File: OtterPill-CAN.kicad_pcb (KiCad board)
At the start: 2 copper layers, 30.8 x 17.6 mm, 19 parts, among them J1 pinh, J2 pinh, J3 CAN, J5 SWD, J7 PAD, U1 TJA1051T-3

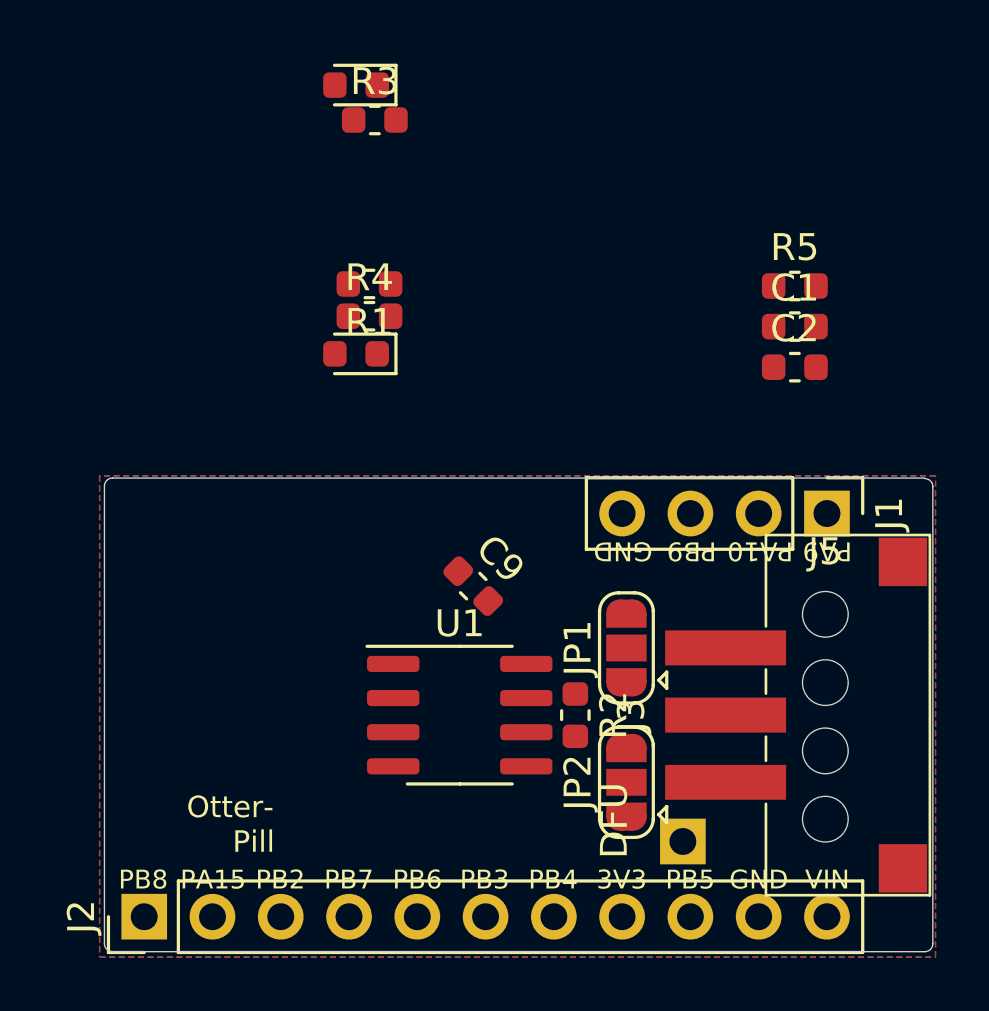
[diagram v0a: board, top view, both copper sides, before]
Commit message: finalized schematic
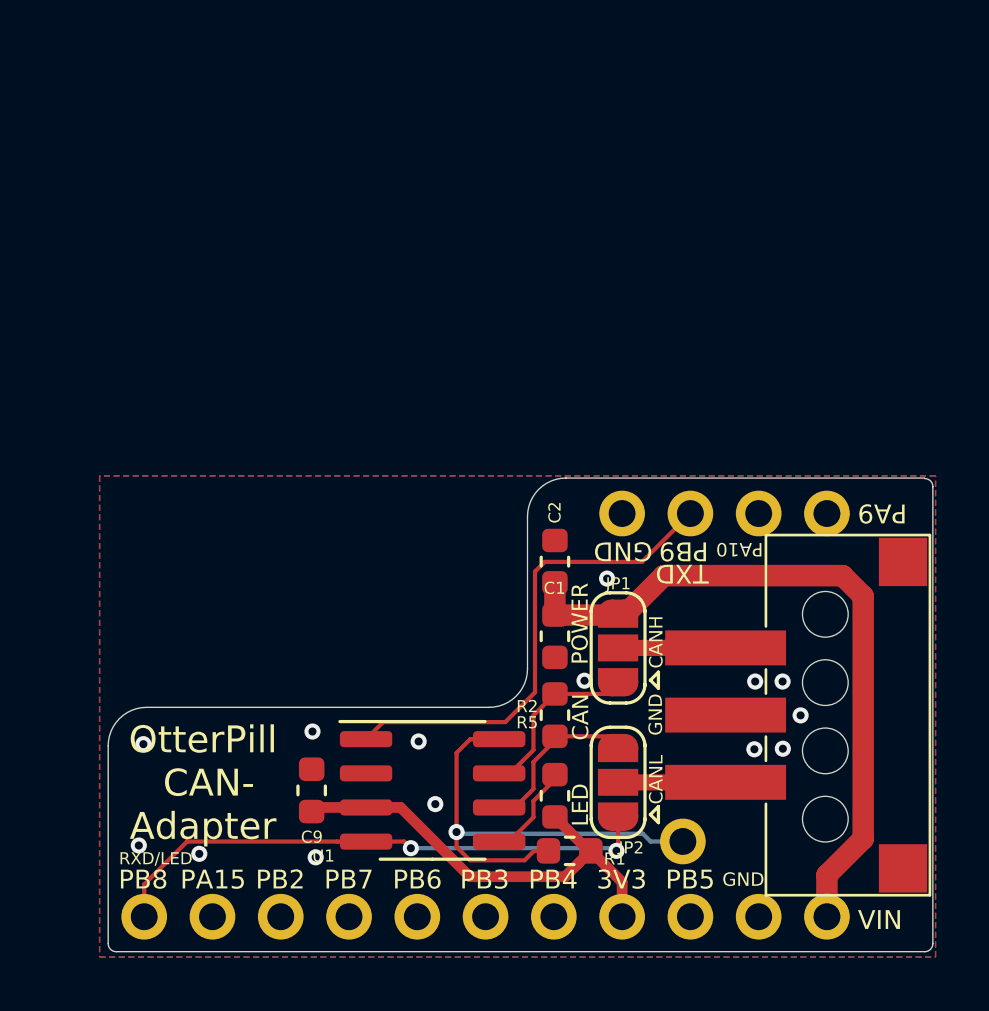
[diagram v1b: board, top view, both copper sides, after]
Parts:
- removed D1: LED RED, LED_SMD:LED_0603_1608Metric
- removed D2: LED GREEN, LED_SMD:LED_0603_1608Metric
- removed R3, R4: 3k3, Resistor_SMD:R_0603_1608Metric
- J1: footprint Connector_PinHeader_2.54mm:PinHeader_1x04_P2.54mm_Vertical -> otter:PinHeader_1x04_P2.54mm_Vertical_NOSILK
- J2: footprint Connector_PinHeader_2.54mm:PinHeader_1x11_P2.54mm_Vertical -> otter:PinHeader_1x11_P2.54mm_Vertical_NOSILK
- J7: footprint Connector_PinHeader_2.54mm:PinHeader_1x01_P2.54mm_Vertical -> otter:PinHeader_1x01_P2.54mm_Vertical_NOSILK
- moved G*** 31.8 mm to (55.1, 55.3)
- moved R1 22.4 mm to (49.7, 33.6)
- moved R5 21.0 mm to (49.1, 31.6), turned to 270 degrees
- moved C1 14.6 mm to (49.1, 25.7), turned to 270 degrees
- moved C2 11.5 mm to (49.1, 22.9), turned to 90 degrees
- moved C9 9.69 mm to (40.1, 31.4), turned to 90 degrees
- moved U1 2.98 mm to (44.6, 31.4)
- moved R2 0.76 mm to (49.1, 28.6)
- moved JP1 0.31 mm to (51.5, 26.1)
- moved JP2 0.31 mm to (51.5, 31.1)
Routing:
- net VIN: track 0.00 -> 26.1 mm
- net RXD: track 0.00 -> 21.0 mm, vias 0 -> 2
- net TXD: track 0.00 -> 18.2 mm
- net Net-(J7-Pad1): track 0.00 -> 17.6 mm, vias 0 -> 1
- net +3V3: track 0.00 -> 16.7 mm
- net Net-(JP1-Pad1): track 0.00 -> 6.88 mm
- net Net-(JP2-Pad3): track 0.00 -> 6.68 mm
- net CAN_L: track 0.00 -> 3.69 mm
- net CAN_H: track 0.00 -> 3.69 mm
- net Net-(R5-Pad1): track 0.00 -> 3.57 mm
- net GND: vias 0 -> 14
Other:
- board size 30.8 x 17.6 mm -> 30.7 x 17.6 mm
- board text added: "CAN"
- board text added: "CANH"
- board text added: "CANL"
- board text added: "LED"
- board text added: "OtterPill CAN- Adapter"
- board text added: "POWER"
- board text added: "RXD/LED"
- board text added: "TXD"
- board text removed: "DFU"
- board text removed: "Otter- Pill"

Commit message: finalized layout
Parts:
- removed C1, C2: 100n 50V, Capacitor_SMD:C_0603_1608Metric
- removed G***: LOGO, otter:otter_laying_3411
- removed JP1: VIN, Jumper:SolderJumper-3_P1.3mm_Open_RoundedPad1.0x1.5mm
- removed JP2: WS2812, Jumper:SolderJumper-3_P1.3mm_Open_RoundedPad1.0x1.5mm
- moved J1 15.0 mm to (59.3, 36.1)
- moved J2 15.0 mm to (33.9, 21.1)
- moved J7 9.40 mm to (53.9, 23.9)
- moved R1 8.86 mm to (51.4, 24.9), turned to 270 degrees
- moved C9 5.87 mm to (42.3, 26.0)
- moved U1 5.87 mm to (46.7, 25.9)
- moved R5 2.33 mm to (51.4, 30.9)
- moved R2 2.32 mm to (51.4, 27.9)
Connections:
- R2 pad 1: Net-(JP1-Pad1) -> CAN_H
- R2 pad 2: Net-(JP2-Pad3) -> CAN_L
- U1 pad 6: Net-(JP2-Pad3) -> CAN_L
- U1 pad 7: Net-(JP1-Pad1) -> CAN_H
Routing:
- net VIN: track 26.1 -> 0.00 mm
- net +3V3: track 16.7 -> 32.5 mm, vias 0 -> 2
- net Net-(J7-Pad1): track 17.6 -> 6.62 mm, vias 1 -> 0
- net Net-(JP1-Pad1): track 6.88 -> 0.00 mm
- net Net-(JP2-Pad3): track 6.68 -> 0.00 mm
- net RXD: track 21.0 -> 15.4 mm, vias 2 -> 0
- net CAN_L: track 3.69 -> 8.57 mm
- net CAN_H: track 3.69 -> 7.64 mm
- net GND: vias 14 -> 17
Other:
- outline, holes or cut-outs redrawn
- rule pad_to_mask_clearance: 0.01 -> 0
- board text added: "Jan Henrik 2019"
- board text removed: "CAN"
- board text removed: "Jan Henrik 2019 v1.2"
- board text removed: "LED"
- board text removed: "Otterpill"
- board text removed: "POWER"
- board text removed: "RXD/LED"
- board text removed: "TXD"
